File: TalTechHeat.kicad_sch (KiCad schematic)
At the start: 74 parts, among them J1 02x03, J2 OLED_SSD1306, J3 XT-30, Q1 DMP4015SPSQ-13, Q2 PJQ4439EP-AU_R2_002A1, Q3 PJQ4439EP-AU_R2_002A1, Q4 IRLR8726TRPBF, Q5 SS8050-G, SW1 Reset_Switch, SW2 BUT1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

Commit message: Exports
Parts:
- J3: MFN (none) -> AMASS; MPN (none) -> XT30PW-F; S1PN (none) -> https://www.tme.eu/en/details/xt30pw-f/dc-power-connectors/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
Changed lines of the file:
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@@
 			)
 		)
-		(property "S1PN" ""
+		(property "S1PN" "https://www.tme.eu/en/details/xt30pw-f/dc-power-connectors/amass/"
 			(at 144.78 209.55 0)
 			(effects
@@
 			)
 		)
-		(property "MFN" ""
+		(property "MFN" "AMASS"
 			(at 144.78 209.55 0)
 			(effects
@@
 			)
 		)
-		(property "MPN" ""
+		(property "MPN" "XT30PW-F"
 			(at 144.78 209.55 0)
 			(effects

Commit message: Updated changes Rev 1.1
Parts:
- SW2, SW3: MFN TE Connectivity / P&B -> Same Sky; MPN 2-1437565-8 -> TS02-66-50-BK-100-LCR-D; S1PN https://www.mouser.ee/ProductDetail/TE-Connectivity-PB/2-14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 -> https://www.mouser.ee/ProductDetail/Same-Sky/TS02-66-50-BK-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
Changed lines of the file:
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@@
 			)
 		)
-		(property "MFN" "TE Connectivity / P&B"
+		(property "MFN" "Same Sky"
 			(at 256.54 261.62 90)
 			(effects
@@
 			)
 		)
-		(property "MPN" " 2-1437565-8 "
+		(property "MPN" " TS02-66-50-BK-100-LCR-D "
 			(at 256.54 261.62 90)
 			(effects
@@
 			)
 		)
-		(property "S1PN" "https://www.mouser.ee/ProductDetail/TE-Connectivity-PB/2-1437565-8?qs=%2FwXgF%2FfIho9gWJ5kkeMo7w%3D%3D"
+		(property "S1PN" "https://www.mouser.ee/ProductDetail/Same-Sky/TS02-66-50-BK-100-LCR-D?qs=A6eO%252BMLsxmQ2%2FFf8jET%252BrA%3D%3D"
 			(at 256.54 261.62 90)
 			(effects
@@
 			)
 		)
+		(property "S1PL" ""
+			(at 256.54 261.62 0)
+			(effects
+				(font
+					(size 1.27 1.27)
+				)
+				(hide yes)
+			)
+		)
+		(property "S1SN" ""
+			(at 256.54 261.62 0)
+			(effects
+				(font
+					(size 1.27 1.27)
+				)
+				(hide yes)
+			)
+		)
 		(pin "1"
 		)
@@
 			)
 		)
-		(property "MFN" "TE Connectivity / P&B"
+		(property "MFN" "Same Sky"
 			(at 218.44 261.62 90)
 			(effects
@@
 			)
 		)
-		(property "MPN" " 2-1437565-8 "
+		(property "MPN" " TS02-66-50-BK-100-LCR-D "
 			(at 218.44 261.62 90)
 			(effects
@@
 			)
 		)
-		(property "S1PN" "https://www.mouser.ee/ProductDetail/TE-Connectivity-PB/2-1437565-8?qs=%2FwXgF%2FfIho9gWJ5kkeMo7w%3D%3D"
+		(property "S1PN" "https://www.mouser.ee/ProductDetail/Same-Sky/TS02-66-50-BK-100-LCR-D?qs=A6eO%252BMLsxmQ2%2FFf8jET%252BrA%3D%3D"
 			(at 218.44 261.62 90)
 			(effects

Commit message: Rev 1.2
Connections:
- net +24V_D is gone; now on net +20V_D: C3.1, U2.4 (EN), U2.5 (VIN)
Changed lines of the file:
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@@
 		(on_board yes)
 		(dnp no)
-		(fields_autoplaced yes)
 		(property "Reference" "#PWR03"
 			(at 100.33 38.1 0)
@@
 			)
 		)
-		(property "Value" "+24V_D"
-			(at 100.33 29.21 0)
+		(property "Value" "+20V_D"
+			(at 96.52 29.21 0)
 			(effects
 				(font
 					(size 1.27 1.27)
 				)
+				(justify left)
 			)
 		)

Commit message: Added the silkscreen as well
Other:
- company: (none) -> Taltech
- title: (none) -> Reflow Plate
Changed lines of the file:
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@@
 	(generator_version "9.0")
 	(paper "A3")
+	(title_block
+		(title "Reflow Plate")
+		(date "2026-01-05")
+		(rev "1.2")
+		(company "Taltech")
+		(comment 1 "Robin Madar")
+		(comment 2 "Taavi Salum")
+	)
 	(rectangle
 		(start 196.85 40.64)

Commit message: Silckscreen changes and BOM changes
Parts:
- C1, C18, C2, C20, C8: Mouser_PN (none) -> 187-CL31B475KBHNFNE; S1PN https://www.mouser.ee/ProductDetail/Samsung-Electro-Mechani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 -> (none)
- C10, C21, C22, C23, C24: Mouser_PN (none) -> 187-CL21B105KBFNNNE; S1PN https://www.mouser.ee/ProductDetail/Samsung-Electro-Mechani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 -> (none)
- C11, C19, C25, C26, C4, C5, C6, C7: Mouser_PN (none) -> 187-CL10B104KC8NNNC; S1PN https://www.mouser.ee/ProductDetail/Samsung-Electro-Mechani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 -> (none)
- C12, C13: Mouser_PN (none) -> 187-CL10C220JB8NNNC; S1PN https://www.mouser.ee/ProductDetail/Samsung-Electro-Mechani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 -> (none)
- C14, C15, C16, C17: Mouser_PN (none) -> 647-UHW1V681MPD; S1PN https://www.mouser.ee/ProductDetail/Nichicon/UHW1V681MPD?qs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 -> (none)
- C3: Mouser_PN (none) -> 187-CL31B225KBHNNNE; S1PN https://www.mouser.ee/ProductDetail/Samsung-Electro-Mechani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 -> (none)
- C9: Mouser_PN (none) -> 187-CL10B103KB8NNNL; S1PN https://www.mouser.ee/ProductDetail/Samsung-Electro-Mechani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 -> (none)
- D1, D5: Mouser_PN (none) -> 833-B5819W-TP; S1PN https://www.mouser.ee/ProductDetail/Micro-Commercial-Compon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 -> (none)
- D2, D4: Mouser_PN (none) -> 595-TSM24ADBZR; S1PN https://www.mouser.ee/ProductDetail/Texas-Instruments/TSM24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 -> (none)
- D3: Mouser_PN (none) -> 621-MBR230S1F-7; S1PN https://www.mouser.ee/ProductDetail/Diodes-Incorporated/MBR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 -> (none)
- J1: Mouser_PN (none) -> 649-1012938190604BLF; S1PN https://www.mouser.ee/ProductDetail/Amphenol-FCI/10129381-9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 -> (none)
- J2: Mouser_PN (none) -> (Endal olemas); S1PN Aliexpress -> (none)
- J3: Mouser_PN (none) -> (Endal olemas); S1PN https://www.tme.eu/en/details/xt30pw-f/dc-power-connectors/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 -> (none)
- L1: Mouser_PN (none) -> 70-IHLP2525BDER8R2M1; S1PN https://www.mouser.ee/ProductDetail/Vishay-Dale/IHLP2525BDE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 -> (none)
- Q1: Mouser_PN (none) -> 621-DMP4015SPSQ-13; S1PN https://www.mouser.ee/ProductDetail/Diodes-Incorporated/DMP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 -> (none)
- Q2, Q3: Mouser_PN (none) -> 241-PJQ4439EP-AUR22A; S1PN https://www.mouser.ee/ProductDetail/Panjit/PJQ4439EP-AU_R2_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 -> (none)
- Q4: Mouser_PN (none) -> 942-IRLR8726TRPBF; S1PN https://www.mouser.ee/ProductDetail/Infineon-Technologies/I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 -> (none)
- Q5: Mouser_PN (none) -> 750-SS8050-G; S1PN https://www.mouser.ee/ProductDetail/Comchip-Technology/SS80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 -> (none)
- R1: Mouser_PN (none) -> 791-RMC16K513FTP; S1PN https://www.mouser.ee/ProductDetail/Kamaya/RMC16K513FTP?qs=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 -> (none)
- R10, R11, R9: Mouser_PN (none) -> 603-RC0603JR-074K7P; S1PN https://www.mouser.ee/ProductDetail/YAGEO/RC0603JR-074K7P?q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 -> (none)
- R12, R16, R22, R7: Mouser_PN (none) -> 71-CRCW06031K00FKEE; S1PN https://www.mouser.ee/ProductDetail/Vishay/CRCW06031K00FKEE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 -> (none)
- R13, R2, R6: Mouser_PN (none) -> 603-RT0603FRE1322K1L; S1PN https://www.mouser.ee/ProductDetail/YAGEO/RT0603FRE1322K1L?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 -> (none)
- R14, R18, R19: Mouser_PN (none) -> 71-RCA0603100KFKEC; S1PN https://www.mouser.ee/ProductDetail/Vishay-Draloric/RCA0603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 -> (none)
- R15: Mouser_PN (none) -> 603-RT0603FRE10100RL; S1PN https://www.mouser.ee/ProductDetail/YAGEO/RT0603FRE10100RL?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 -> (none)
- R17: Mouser_PN (none) -> 603-AC0603JR-7W470RL; S1PN https://www.mouser.ee/ProductDetail/YAGEO/AC0603JR-7W470RL?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 -> (none)
- R20, R21, R24, R25, R26: Mouser_PN (none) -> 603-AF0603FR-0710KL; S1PN https://www.mouser.ee/ProductDetail/YAGEO/AF0603FR-0710KL?q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 -> (none)
- R23: Mouser_PN (none) -> 603-AF0603FR-074K7L; S1PN https://www.mouser.ee/ProductDetail/YAGEO/AF0603FR-074K7L?q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 -> (none)
- R3, R4: Mouser_PN (none) -> 791-RMC1/16K22R0FTP; S1PN https://www.mouser.ee/ProductDetail/Kamaya/RMC1-16K22R0FTP?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 -> (none)
- R5, R8: Mouser_PN (none) -> 603-AF0603FR-0710KL %3D; S1PN https://www.mouser.ee/ProductDetail/YAGEO/AF0603FR-0710KL?q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 -> (none)
- SW1: Mouser_PN (none) -> 710-434133025816; S1PN https://www.mouser.ee/ProductDetail/Wurth-Elektronik/434133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 -> (none)
- SW2, SW3: Mouser_PN (none) -> 179-TS026650BK100LCR; S1PN https://www.mouser.ee/ProductDetail/Same-Sky/TS02-66-50-BK-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 -> (none)
- U1: Mouser_PN (none) -> 511-STM32F103C6T7A; S1PN https://www.mouser.ee/ProductDetail/STMicroelectronics/STM3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 -> (none)
- U2: Mouser_PN (none) -> 621-AP64060ZQWU-7; S1PN https://www.mouser.ee/ProductDetail/Diodes-Incorporated/AP6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 -> (none)
- U3: Mouser_PN (none) -> 640-USB4085-GF-A; S1PN https://www.mouser.ee/ProductDetail/GCT/USB4085-GF-A?qs=KUo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 -> (none)
- U4: Mouser_PN (none) -> 511-STUSB4500QTR; S1PN https://www.mouser.ee/ProductDetail/STMicroelectronics/STUS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 -> (none)
- Y1: Mouser_PN (none) -> 520-80-12-33Q-GN-TR; S1PN https://www.mouser.ee/ProductDetail/ECS/ECS-80-12-33Q-GN-TR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 -> (none)

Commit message: Rev 1.3, one resistor and exports update
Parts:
- added R27: 1k, Resistor_SMD:R_0603_1608Metric_Pad0.98x0.95mm_HandSolder, symbol ScottoKeebs:Placeholder_Resistor
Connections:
- net +3.3V: now also R27.2
- net U_P: now also R27.1
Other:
- moved on the sheet: R3, R4

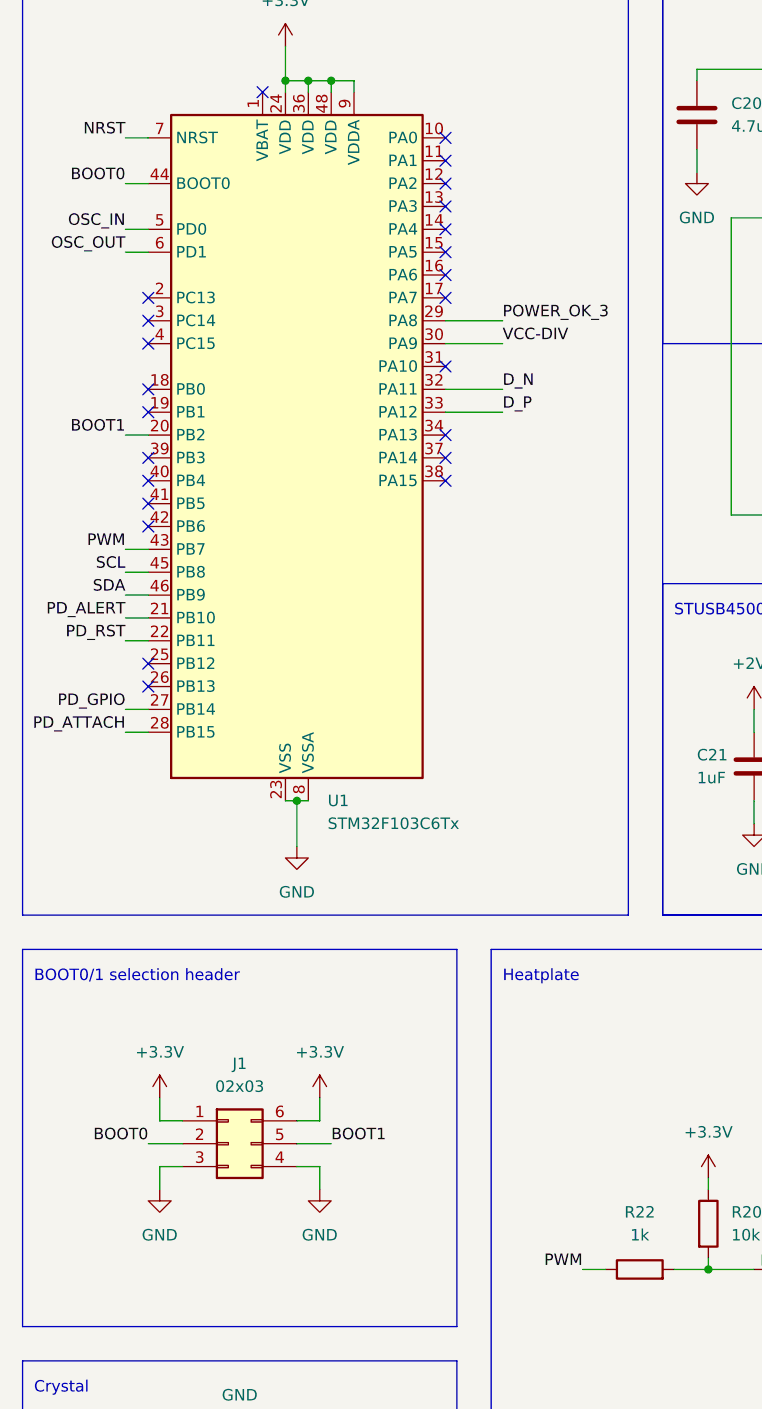
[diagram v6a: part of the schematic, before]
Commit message: Removed boot1, added UART
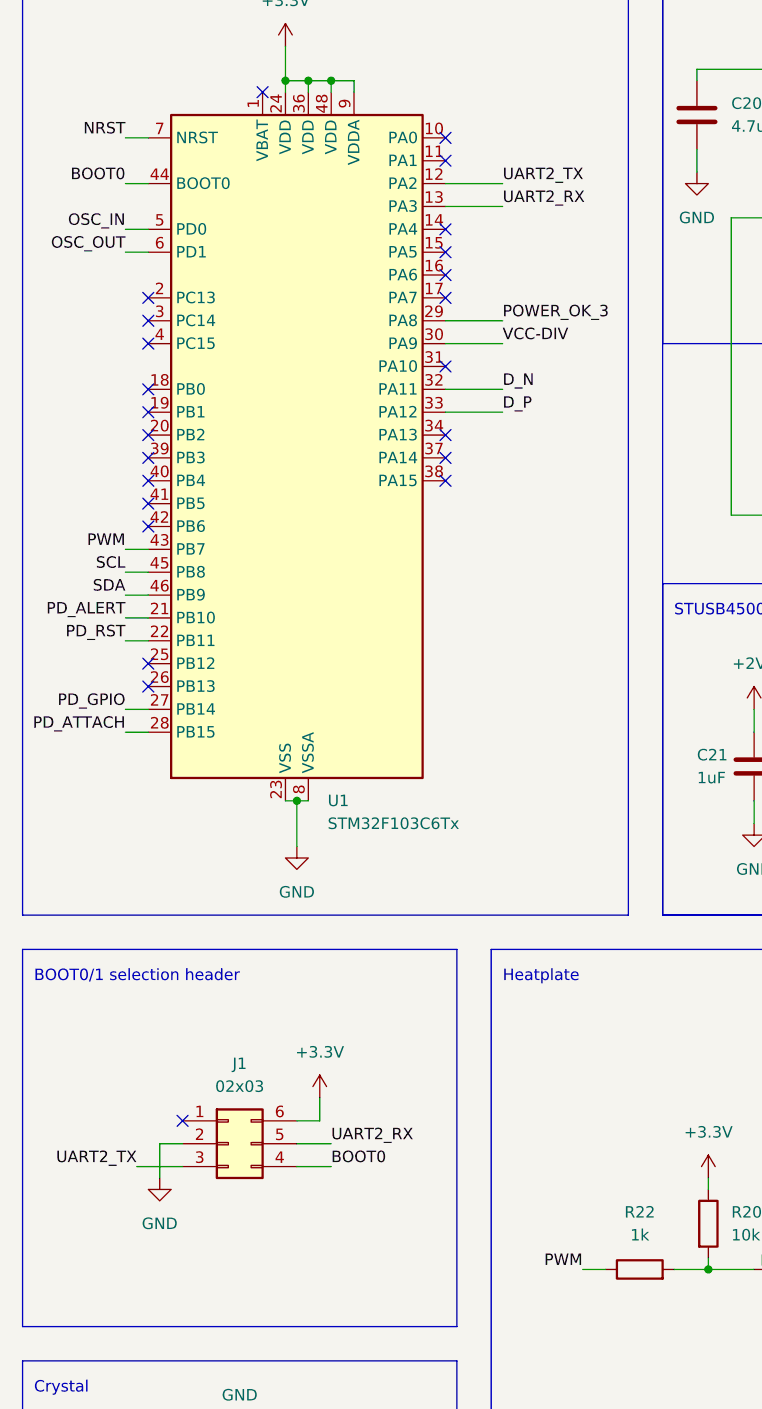
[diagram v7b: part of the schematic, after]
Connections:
- net +3.3V: no longer J1.1 (Pin_1)
- net BOOT0: now also J1.4 (Pin_4); no longer J1.2 (Pin_2)
- net GND: now also J1.2 (Pin_2); no longer J1.3 (Pin_3), J1.4 (Pin_4)
- net UART2_TX: now reaches U1.12 (PA2)
- net UART2_TX: now also J1.3 (Pin_3)
- net UART2_RX: now reaches U1.13 (PA3)
- net UART2_RX: now also J1.5 (Pin_5)
- net BOOT1: no longer names the net of U1.20 (PB2)
- net BOOT1: no longer J1.5 (Pin_5)

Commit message: TaltechPlate folder Rev1, no Titleblock yet
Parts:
- added J4: Conn_01x04, Connector_JST:JST_PH_B4B-PH-K_1x04_P2.00mm_Vertical, symbol Connector_Generic:Conn_01x04
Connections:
- net +3.3V: now also J4.1 (Pin_1)
- net GND: now also J4.4 (Pin_4)
- net TEMP_1: now reaches U1.14 (PA4)
- net TEMP_1: now also J4.2 (Pin_2)
- net TEMP_2: now reaches U1.15 (PA5)
- net TEMP_2: now also J4.3 (Pin_3)
- no-connect marks 28 -> 26
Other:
- note added: "Temperature sensors"
